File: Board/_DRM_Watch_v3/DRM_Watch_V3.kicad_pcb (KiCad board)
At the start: 2 copper layers, 62.7 x 44.4 mm, 81 parts, among them J1 TYPE-C-31-M-12, J2 687110149022, Q1 2N7002LT1G, U1 ESP32-S2, U3 TP4056, Y1 XRCGB48M000F0Z00R0

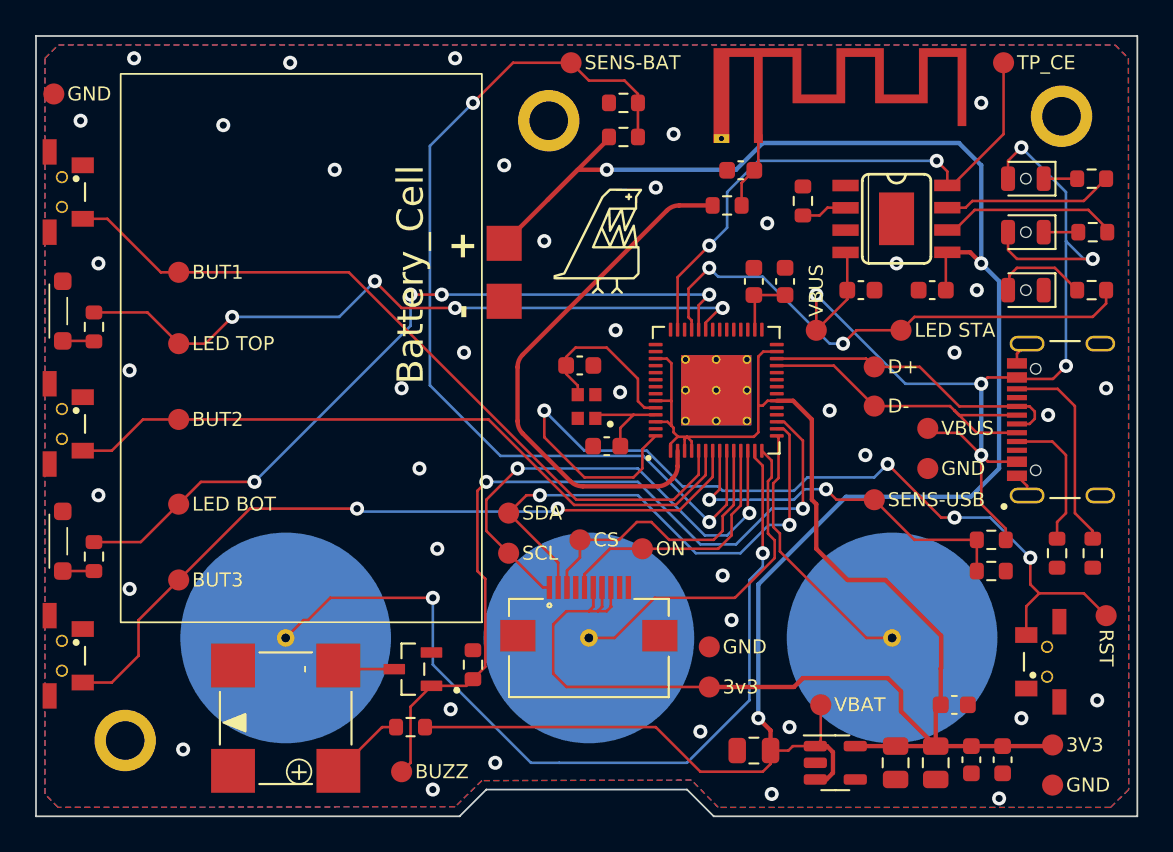
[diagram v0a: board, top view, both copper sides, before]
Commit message: 2024-01-15 Board: add step-up resistor and cap to RST pin 2024-01-15 Board: quartz bigger package 2024-01-15 Board: add more testpoints for unused pins 2024-01-15 Board: top led: place for smaller led 2024-01-15 Board: move caacitors closer to chips 2024-01-15 Board: make wifi wire thicker 2024-01-15 Board: move wifi antenna closer to chips 2024-01-15 Board: add vias around ANT wire 2024-01-15 Board: move antenna elements closer to chip  2024-01-15 Board: replace onboard antenna by wire soldered on board 2024-01-15 Board: Add jumper to close charger 2024-01-15 Board: Add dm123a chip    (static const uint8_t SDA = 33;   static const uint8_t SCL = 35;)
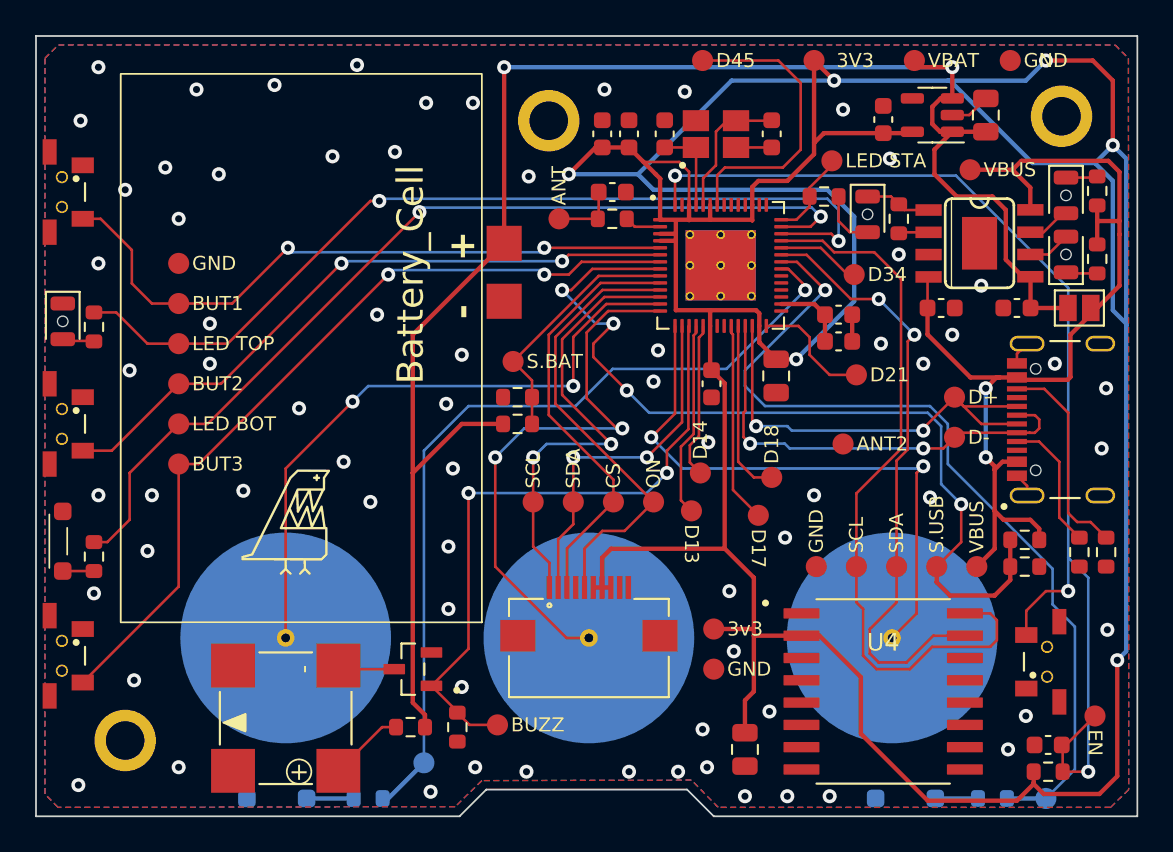
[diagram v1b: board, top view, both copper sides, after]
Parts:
- removed AE1: Antenna, Project-Lib:Texas_SWRA117D_2.4GHz_Right
- added C14: 1uF, Project-Lib:C_0603_1608Metric, F.Cu at (123.7, 83.6)
- added C15: 10uF, Project-Lib:C_0603_1608Metric, F.Cu at (98.3, 48.8)
- added D6: BL1, Project-Lib:SMD-LED-Side-View, B.Cu at (79.8, 86.6)
- added D7: BL2, Project-Lib:SMD-LED-Side-View, B.Cu at (115.6, 86.6)
- added G***: LOGO, Project-Lib:zubat_v5, B.Cu at (90.9, 51.8)
- added JP1: Jumper_2_Open, Project-Lib:SolderJumper-2_P1.3mm_Open_Pad1.0x1.5mm, F.Cu at (125.5, 58.7)
- added R16: 10K, Project-Lib:R_0603_1608Metric, F.Cu at (123.7, 85.1)
- added R17: R22, Project-Lib:R_0603_1608Metric, B.Cu at (85.0, 86.6)
- added R18: R22, Project-Lib:R_0603_1608Metric, B.Cu at (120.5, 86.6)
- added TP27: ANT, Project-Lib:TestPoint_Pad, F.Cu at (95.8, 53.6)
- added TP28: ANT2, Project-Lib:TestPoint_Pad, F.Cu at (112.0, 66.4)
- added TP29: SDA, Project-Lib:TestPoint_Pad, F.Cu at (115.1, 73.4)
- added TP30: SCL, Project-Lib:TestPoint_Pad, F.Cu at (112.8, 73.4)
- added TP31: D14, Project-Lib:TestPoint_Pad, F.Cu at (103.9, 68.1)
- added TP32: D17, Project-Lib:TestPoint_Pad, F.Cu at (107.2, 70.5)
- added TP33: D18, Project-Lib:TestPoint_Pad, F.Cu at (108.0, 68.3)
- added TP34: D21, Project-Lib:TestPoint_Pad, F.Cu at (112.8, 62.5)
- added TP35: D45, Project-Lib:TestPoint_Pad, F.Cu at (104.0, 44.6)
- added TP36: D34, Project-Lib:TestPoint_Pad, F.Cu at (112.6, 56.8)
- added TP37: D13, Project-Lib:TestPoint_Pad, F.Cu at (103.4, 70.2)
- added TP38: BL2, Project-Lib:TestPoint_Pad, B.Cu at (123.6, 86.6)
- added U4: DS3231S, Project-Lib:SOIC127P1032X265-16N, F.Cu at (114.3, 80.5)
- D1: footprint Project-Lib:SMD-LED-Side-View -> Project-Lib:HOLE_LED_0805_2012Metric
- TP10: value RST -> EN
- TP11: value SENS-BAT -> S.BAT
- TP12: value SENS-USB -> S.USB
- TP26: value TP_CE -> BL1; moved to B.Cu
- moved TP26 51.8 mm to (88.1, 84.6), turned to 180 degrees
- moved C5 41.5 mm to (99.8, 48.8), turned to 90 degrees
- moved TP9 41.3 mm to (121.5, 44.6)
- moved TP1 41.3 mm to (110.4, 44.6), turned to -90 degrees
- moved C9 38.5 mm to (120.1, 47.7), turned to 90 degrees
- moved U2 37.3 mm to (117.1, 47.7), turned to 180 degrees
- moved TP2 37.1 mm to (116.1, 44.6)
- moved C6 33.6 mm to (114.3, 47.9), turned to 90 degrees
- moved C4 26.0 mm to (104.5, 63.0)
- moved G*** 23.9 mm to (80.3, 70.9)
- moved C1 23.8 mm to (108.2, 62.5)
- moved C2 18.1 mm to (101.9, 48.8), turned to -90 degrees
- moved R12 17.8 mm to (93.5, 63.8)
- moved R11 17.4 mm to (93.5, 65.3)
- moved TP11 17.3 mm to (93.2, 61.7)
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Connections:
- D3 pad 2: VBUS -> Net-(D3-A)
- D4 pad 2: VBUS -> Net-(D4-A)
- R10 pad 2: Net-(U1-GPIO35) -> Net-(U1-GPIO38)
- R5 pad 2: Net-(U1-GPIO33) -> Net-(U1-GPIO36)
- R6 pad 2: Net-(U1-GPIO34) -> Net-(U1-GPIO37)
- R7 pad 1: Net-(U3-STDBY) -> VBUS
- R8 pad 1: Net-(U3-CHRGE) -> VBUS
- TP19 pad 1: Net-(U1-GPIO33) -> Net-(U1-GPIO36)
- TP20 pad 1: Net-(U1-GPIO34) -> Net-(U1-GPIO37)
- TP21 pad 1: Net-(U1-GPIO35) -> Net-(U1-GPIO38)
- TP26 pad 1: Net-(U1-GPIO37) -> Net-(U1-SPIQ/GPIO31)
- U1 pad 18: unconnected-(U1-GPIO13/ADC2_CH2-Pad18) -> Net-(U1-GPIO13/ADC2_CH2)
- U1 pad 19: unconnected-(U1-GPIO14/ADC2_CH3-Pad19) -> Net-(U1-GPIO14/ADC2_CH3)
- U1 pad 23: unconnected-(U1-GPIO17/ADC2_CH6/DAC_1-Pad23) -> Net-(U1-GPIO17/ADC2_CH6/DAC_1)
- U1 pad 24: unconnected-(U1-GPIO18/ADC2_CH7/DAC_2-Pad24) -> Net-(U1-GPIO18/ADC2_CH7/DAC_2)
- U1 pad 28: unconnected-(U1-GPIO21-Pad28) -> Net-(U1-GPIO21)
- U1 pad 35: unconnected-(U1-SPIQ/GPIO31-Pad35) -> Net-(U1-SPIQ/GPIO31)
- U1 pad 36: unconnected-(U1-SPID/GPIO32-Pad36) -> Net-(U1-SPID/GPIO32)
- U1 pad 40: unconnected-(U1-GPIO36-Pad40) -> Net-(U1-GPIO36)
- U1 pad 42: unconnected-(U1-GPIO38-Pad42) -> Net-(U1-GPIO38)
- U1 pad 50: unconnected-(U1-GPIO45-Pad50) -> Net-(U1-GPIO45)
- U3 pad 6: Net-(U3-STDBY) -> Net-(D3-A)
- U3 pad 7: Net-(U3-CHRGE) -> Net-(D4-A)
- U3 pad 8: Net-(U1-GPIO37) -> VBUS
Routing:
- net +3V3: track 93.2 -> 240.1 mm, vias 0 -> 6
- net Net-(U1-GPIO36): track 0.00 -> 52.1 mm, vias 0 -> 2
- net Net-(U1-SPID/GPIO32): track 0.00 -> 50.2 mm, vias 0 -> 1
- net Net-(U1-SPIQ/GPIO31): track 0.00 -> 48.5 mm, vias 0 -> 1
- net Net-(U1-GPIO4/ADC1_CH3): track 54.2 -> 14.4 mm, vias 2 -> 0
- net Net-(U1-GPIO34): track 44.2 -> 4.79 mm, vias 4 -> 0
- net Net-(U1-GPIO3/ADC1_CH2): track 21.5 -> 50.7 mm, vias 2 -> 4
- net Net-(U1-LNA_IN/RF): track 30.5 -> 2.09 mm
- net Net-(U1-GPIO37): track 31.8 -> 53.6 mm
- net Net-(T3-touch): track 15.3 -> 33.7 mm, vias 0 -> 2
- net Net-(U1-GPIO45): track 0.00 -> 17.0 mm
- net VCC: track 113.8 -> 97.8 mm, vias 3 -> 2
- net Net-(U1-CHIP_PU/RESET): track 52.1 -> 66.5 mm, vias 4 -> 3
- net Net-(T2-touch): track 19.1 -> 32.3 mm, vias 0 -> 2
- net Net-(T1-touch): track 49.7 -> 36.5 mm
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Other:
- board text added: "DRM Watch V3"
- board text added: "Designed by Dr.Failov"
- board text added: "Made in Ukraine"
- board text added: "Rev.2 (2024-01-15)"
- board text removed: "Rev: 20231220"

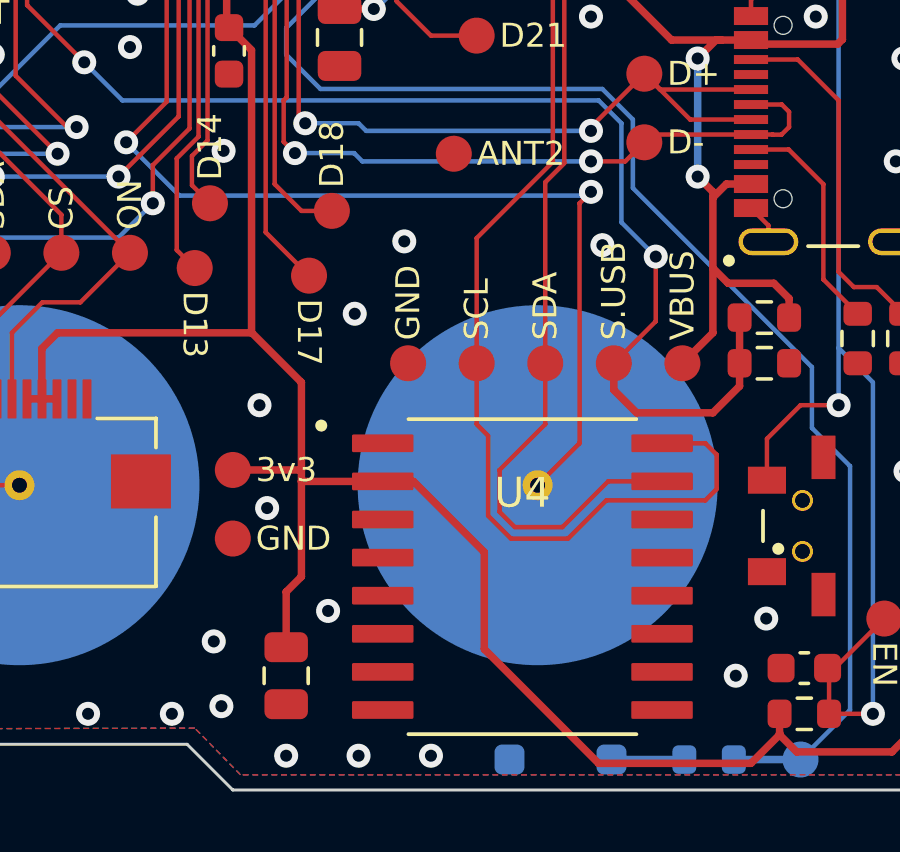
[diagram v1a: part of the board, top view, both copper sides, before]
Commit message: 2024-02-03 v0.23 Stopwatch fixed 2024-02-03 v0.23 updated init led effect 2024-02-03 v0.23 added value showing time since last charging 2024-02-03 v0.23 replaced back icon 2024-02-03 v0.23 started implementing of alert functionality
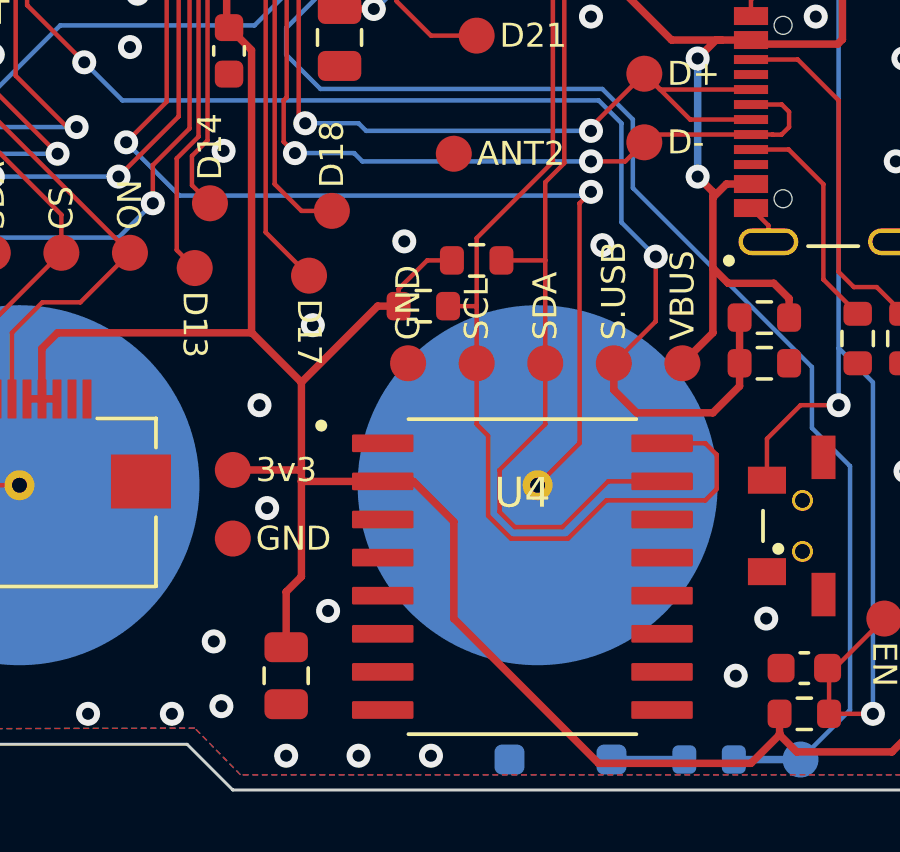
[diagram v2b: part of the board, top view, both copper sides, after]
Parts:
- added R19: 4.3K, Project-Lib:R_0603_1608Metric, F.Cu at (112.8, 70.0)
- added R20: 4.3K, Project-Lib:R_0603_1608Metric, F.Cu at (111.0, 71.5)
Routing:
- net +3V3: track 240.1 -> 247.1 mm
- net Net-(U1-GPIO33): track 34.9 -> 36.4 mm
- net Net-(U1-GPIO35): track 42.1 -> 43.1 mm

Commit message: bosrd
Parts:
- removed D6: BL1, Project-Lib:SMD-LED-Side-View
- removed D7: BL2, Project-Lib:SMD-LED-Side-View
- removed R17, R18: R22, Project-Lib:R_0603_1608Metric
- removed T1, T2, T3: ~, Project-Lib:Touch-Region
- removed TP26: BL1, Project-Lib:TestPoint_Pad
- removed TP38: BL2, Project-Lib:TestPoint_Pad
- added C16: 12nF 200V, Capacitor_SMD:C_1206_3216Metric, F.Cu at (139.2, 58.3)
- added U5: ~, Package_DFN_QFN:QFN-16-1EP_4x4mm_P0.65mm_EP2.5x2.5mm, F.Cu at (139.5, 53.5)
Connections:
- U1 pad 13: Net-(T1-touch) -> unconnected-(U1-GPIO8/ADC1_CH7-Pad13)
- U1 pad 14: Net-(T2-touch) -> unconnected-(U1-GPIO9/ADC1_CH8-Pad14)
- U1 pad 15: Net-(T3-touch) -> unconnected-(U1-GPIO10/ADC1_CH9-Pad15)
- U1 pad 23: Net-(U1-GPIO17/ADC2_CH6/DAC_1) -> unconnected-(U1-GPIO17/ADC2_CH6/DAC_1-Pad23)
- U1 pad 35: Net-(U1-SPIQ/GPIO31) -> unconnected-(U1-SPIQ/GPIO31-Pad35)
- U1 pad 36: Net-(U1-SPID/GPIO32) -> unconnected-(U1-SPID/GPIO32-Pad36)
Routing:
- net Net-(U1-SPID/GPIO32): track 50.2 -> 0.00 mm, vias 1 -> 0
- net Net-(U1-SPIQ/GPIO31): track 48.5 -> 0.00 mm, vias 1 -> 0
- net Net-(T1-touch): track 36.5 -> 0.00 mm, vias 2 -> 0
- net Net-(T3-touch): track 33.7 -> 0.00 mm, vias 2 -> 0
- net Net-(T2-touch): track 32.3 -> 0.00 mm, vias 2 -> 0
- net unconnected-(U1-SPID/GPIO32-Pad36): track 0.00 -> 3.17 mm, vias 0 -> 1
- net Net-(D6-A): track 2.68 -> 0.00 mm
- net Net-(D7-A): track 2.43 -> 0.00 mm

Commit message: 2024-02-25 Board: Added symbols for HV857 2024-02-26 Board: Added case outline to board project 2024-02-26 Schematic: Added elements for EL Backlight
2024-02-25 Board: Added symbols for HV857
2024-02-26 Board: Added case outline to board project
2024-02-26 Schematic: Added elements for EL Backlight
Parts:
- added C17: 4.7uF, Project-Lib:C_1206, F.Cu at (148.0, 64.2)
- added C18: 0.1uF, Project-Lib:C_1206, F.Cu at (148.0, 67.6)
- added D6: US1D, Diode_SMD:D_SMA, F.Cu at (149.3, 60.3)
- added L1: 220uH, Project-Lib:Inductor-L_1210_3225Metric, F.Cu at (153.7, 64.6)
- added R17: 560K, Project-Lib:R_0603_1608Metric, F.Cu at (139.1, 44.6)
- added R18: 2M, Project-Lib:R_0603_1608Metric, F.Cu at (139.1, 47.1)
- added R21: 500R, Project-Lib:R_0603_1608Metric, F.Cu at (152.9, 68.0)
- added TP26: EL1, Project-Lib:TestPoint_Pad, F.Cu at (147.1, 49.9)
- added TP38: BLEN, Project-Lib:TestPoint_Pad, F.Cu at (142.7, 45.0)
- C16: footprint Capacitor_SMD:C_1206_3216Metric -> Project-Lib:C_1206
- TP32: value D17 -> EL2
- U5: footprint Package_DFN_QFN:QFN-16-1EP_4x4mm_P0.65mm_EP2.5x2.5mm -> Project-Lib:HV857
- moved TP32 43.5 mm to (146.9, 52.7)
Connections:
- C16 pad 1: unconnected-(C16-Pad1) -> Net-(D6-K)
- C16 pad 2: unconnected-(C16-Pad2) -> GND
- TP32 pad 1: Net-(U1-GPIO17/ADC2_CH6/DAC_1) -> Net-(U5-VB)
- U1 pad 13: unconnected-(U1-GPIO8/ADC1_CH7-Pad13) -> Net-(U1-GPIO8/ADC1_CH7)
- U5 pad 1: unconnected-(U5-RSW-Osc-Pad1) -> +3V3
- U5 pad 2: unconnected-(U5-REL-Osc-Pad2) -> Net-(U5-RSW-Osc)
- U5 pad 3: unconnected-(U5-SEL-Pad3) -> Net-(U5-REL-Osc)
- U5 pad 4: unconnected-(U5-VREG-Pad4) -> GND
- U5 pad 5: unconnected-(U5-VOUT-Pad5) -> Net-(D6-A)
- U5 pad 6: unconnected-(U5-VDD-Pad6) -> Net-(D6-K)
- U5 pad 7: unconnected-(U5-GND-Pad7) -> Net-(U5-VB)
- U5 pad 8: unconnected-(U5-RSLEW-OUT-Pad8) -> Net-(U5-VA)
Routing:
- net Net-(U1-GPIO17/ADC2_CH6/DAC_1): track 11.4 -> 0.00 mm
